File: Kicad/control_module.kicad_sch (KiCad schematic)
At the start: 0 parts

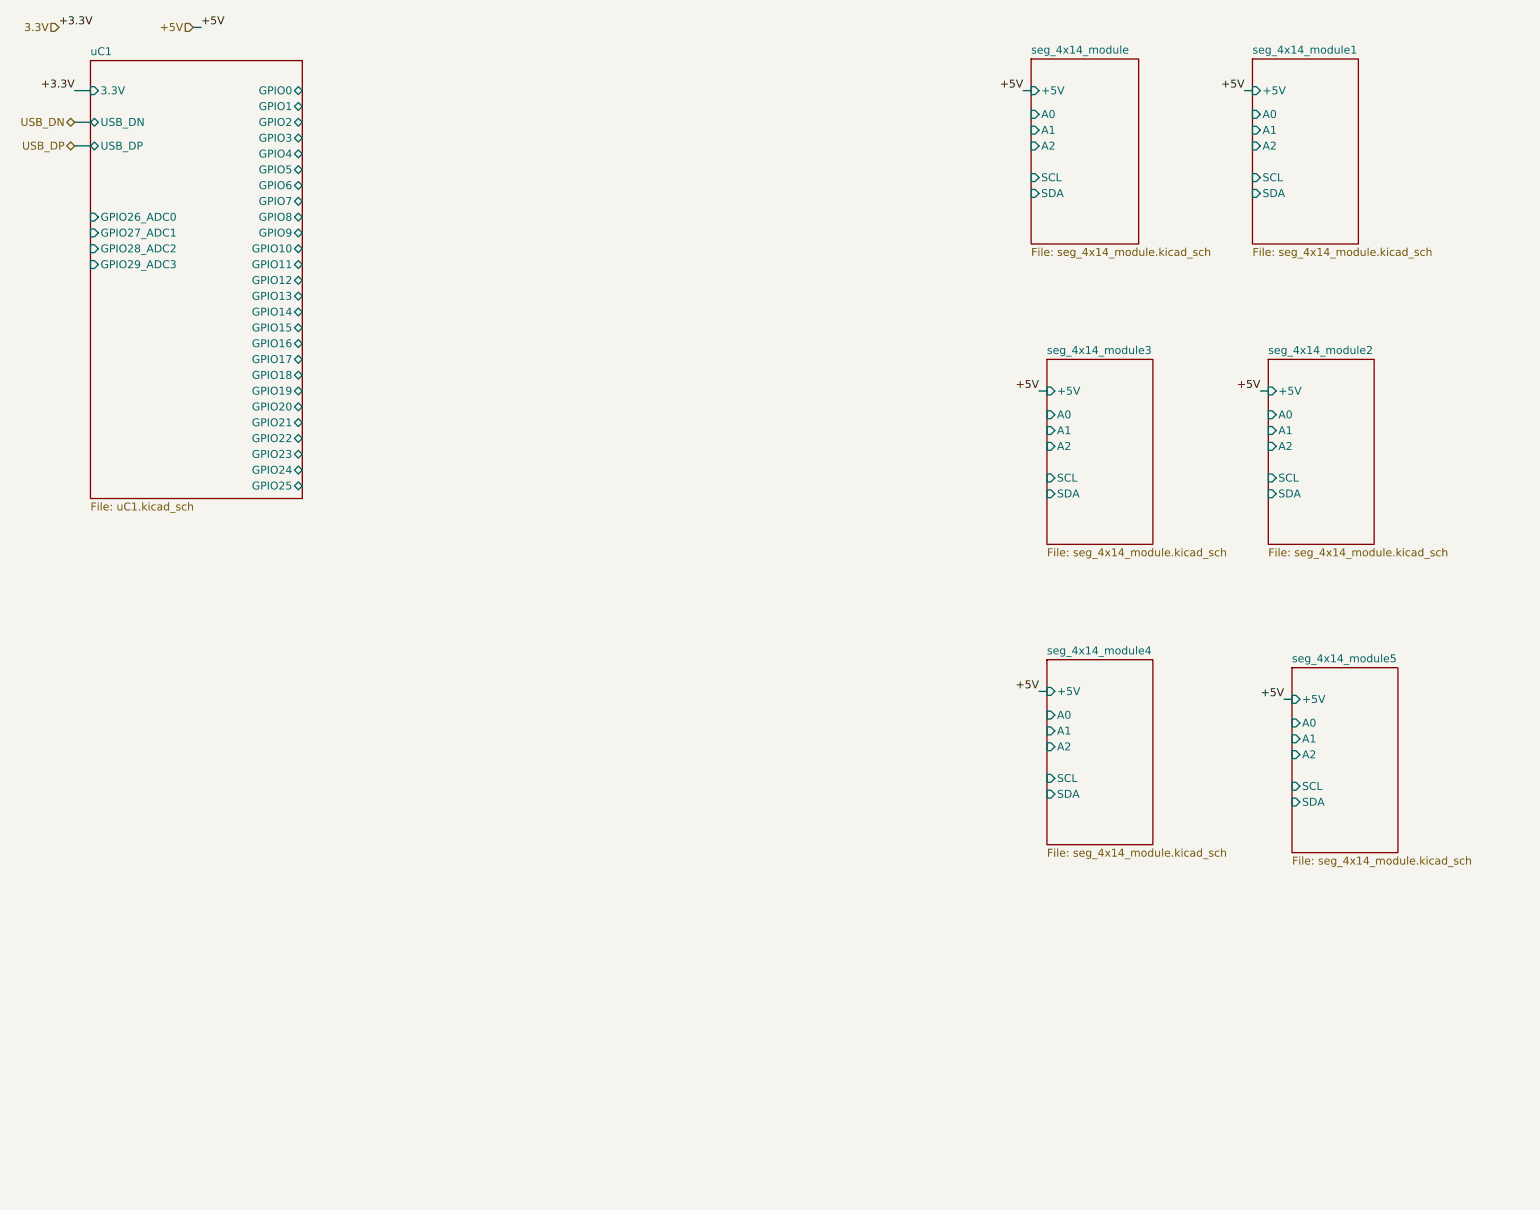
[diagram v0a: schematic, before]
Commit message: adding multiple component (14 semgent and led)
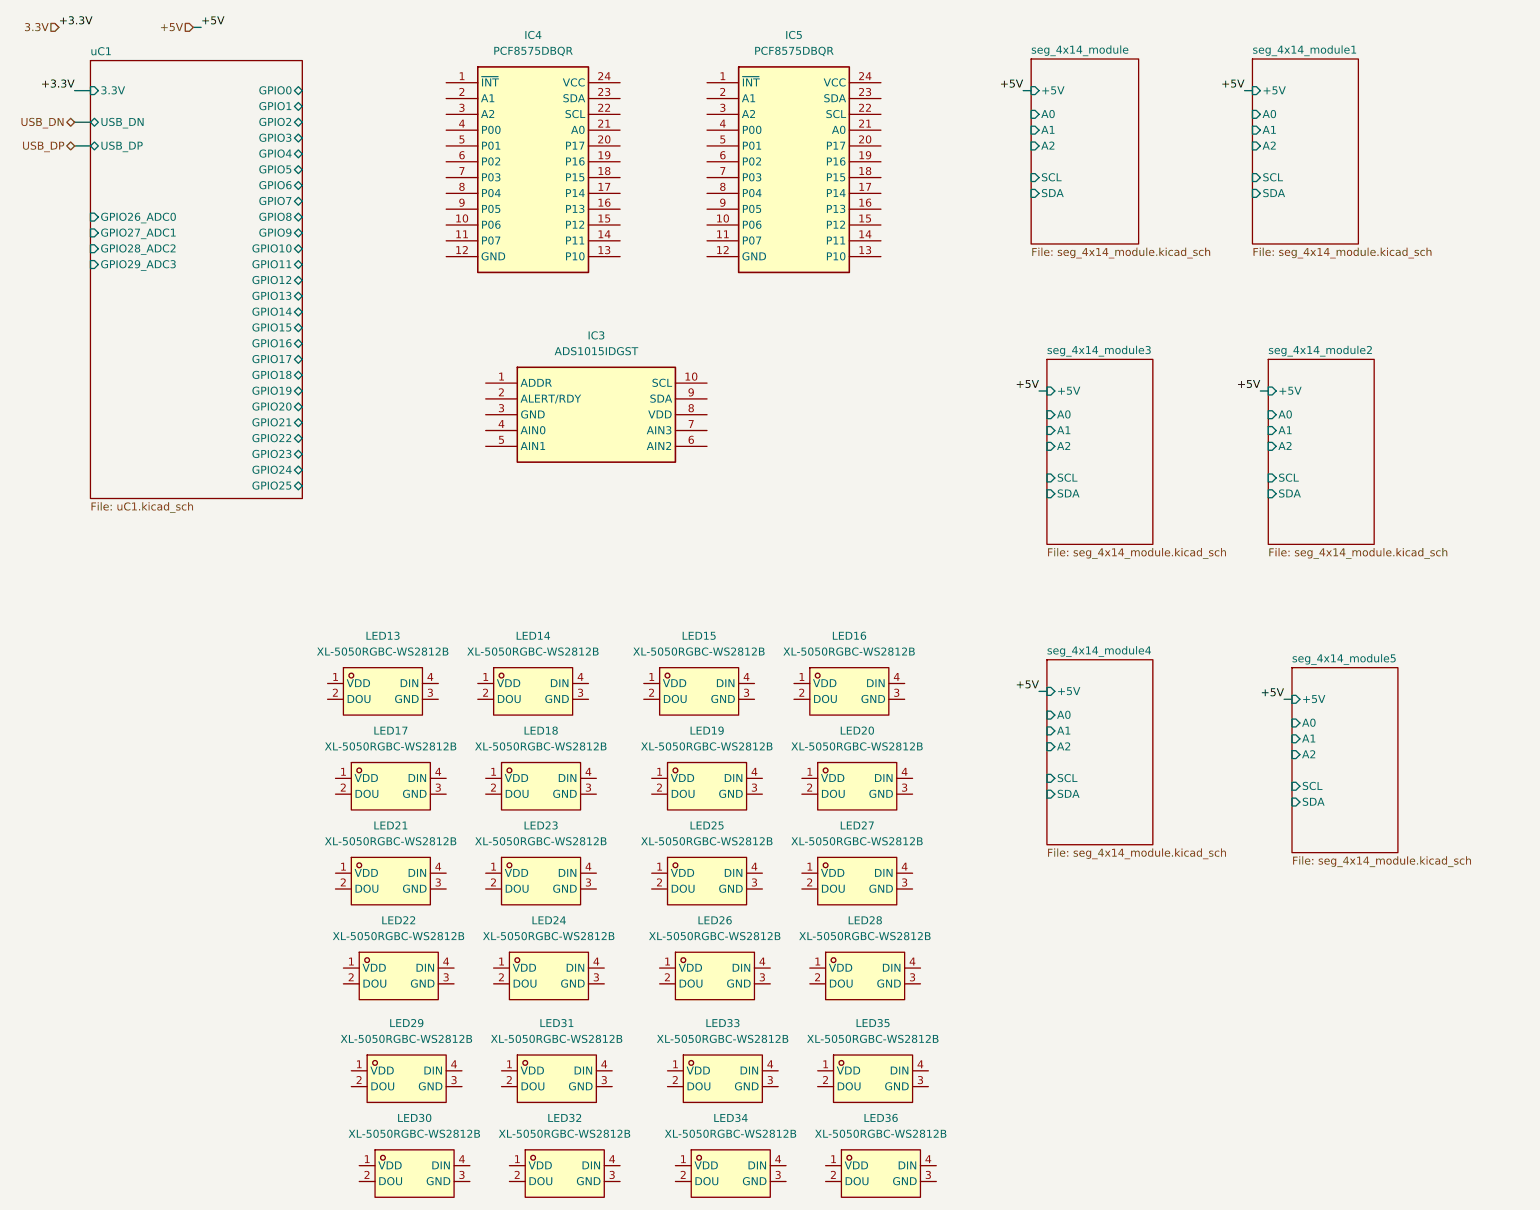
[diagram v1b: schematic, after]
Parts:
- added IC3: ADS1015IDGST, Eeloo_Pad:SOP50P490X110-10N, symbol Eeloo_Pad:ADS1015IDGST
- added IC4, IC5: PCF8575DBQR, Eeloo_Pad:SOP64P600X175-24N, symbol Eeloo_Pad:PCF8575DBQR
- added LED13, LED14, LED15, LED16, LED17, LED18, LED19, LED20, LED21, LED22, LED23, LED24, LED25, LED26, LED27, LED28, LED29, LED30, LED31, LED32, LED33, LED34, LED35, LED36: XL-5050RGBC-WS2812B, Eeloo_Pad:LED-SMD_4P-L5.0-W5.0-BL_XL-5050RGBC, symbol Eeloo_Pad:XL-5050RGBC-WS2812B

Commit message: working on the 14 segment schematics
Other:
- sheet seg_4x14_module ports: added A0_1, A0_2, A1_1, A1_2, A2_1, A2_2; removed A0, A1, A2
- sheet seg_4x14_module1 ports: added A0_1, A0_2, A1_1, A1_2, A2_1, A2_2; removed A0, A1, A2
- sheet seg_4x14_module2 ports: added A0_1, A0_2, A1_1, A1_2, A2_1, A2_2; removed A0, A1, A2
- sheet seg_4x14_module3 ports: added A0_1, A0_2, A1_1, A1_2, A2_1, A2_2; removed A0, A1, A2
- sheet seg_4x14_module4 ports: added A0_1, A0_2, A1_1, A1_2, A2_1, A2_2; removed A0, A1, A2
- sheet seg_4x14_module5 ports: added A0_1, A0_2, A1_1, A1_2, A2_1, A2_2; removed A0, A1, A2
